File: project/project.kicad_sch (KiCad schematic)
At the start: 174 parts

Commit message: adding more things
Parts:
- removed Cs19, Cs20: chair s, -local:chair_small, symbol Device:R
- removed R83: clean clothes, -local:_o_clean_clothes__, symbol Device:R
- added R12: Painting table, -local:_o_painting_table__, symbol Device:R
- added R20: palet rack2, -local:_o_palet_rack__, symbol Device:R
- added R21: Broken tools, -local:_o_broken_tools_shelf__, symbol Device:R
- added R22: Strings and wheels, -local:_o_strings_wheels_shelf__, symbol Device:R
- added R39: cube container, -local:_o_cube_container__, symbol Device:R
- added R45: Trash el, -local:_o_trash_electronics__, symbol Device:R
- added R55: Dirty small table, -local:_o_dirty_small_table__, symbol Device:R
- added R58: Presentation chairs, -local:_o_chair_box__, symbol Device:R
- added R65: Lightbox, -local:_e_lightbox__, symbol Device:R
- added R80: el center shitty table, -local:_e_shitty_table__, symbol Device:R
- R19: renamed from R35; value palet rack -> palet rack1
- R68: renamed from R78; footprint -local:_e_kitchen_table2__ -> -local:_e_shitty_table__
- R73: renamed from R69; footprint -local:_e_lab_table_x3__ -> -local:_e_lab_table_normal__
- R74: renamed from R70; footprint -local:_e_lab_table_x3__ -> -local:_e_lab_table_tall__
- R75: renamed from R71; footprint -local:_e_lab_table_x3__ -> -local:_e_lab_table_tall__
- R78: renamed from R74; footprint -local:_e_center_table2__ -> -local:_e_center_table1__
- R99: renamed from R90; footprint -local:_o_rack__ -> -local:_e_rack__
- renumbered R12 to R13, R13 to R14, R14 to R17, R36 to R18, R19 to R23, R20 to R24, R21 to R25, R22 to R26, R23 to R27, R24 to R28, R25 to R29, R26 to R30, R27 to R31, R28 to R32, R29 to R33, R30 to R34, R31 to R35, R32 to R36, R33 to R37, R34 to R38, R37 to R40, R38 to R41, R39 to R42, R40 to R43, R41 to R44, R42 to R46, R43 to R47, R44 to R48, R45 to R49, R46 to R50, R47 to R51, R48 to R52, R18 to R53, R17 to R54, R49 to R56, R50 to R57, R51 to R59, R52 to R60, R53 to R61, R54 to R62, R55 to R63, R56 to R64, R76 to R66, R77 to R67, R79 to R69, R80 to R70, R81 to R71, R82 to R72, R72 to R76, R73 to R77, R75 to R79, R57 to R81, R58 to R82, R59 to R83, R60 to R84, R61 to R85, R62 to R86, R63 to R87, R64 to R88, R65 to R89, R66 to R90, R67 to R91, R68 to R92, R84 to R93, R85 to R94, R86 to R95, R87 to R96, R88 to R97, R89 to R98

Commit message: moving things around
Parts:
- removed Be8: bench, -local:_e_bench__, symbol Device:R
- removed R34: hammers, -local:_o_thin_shelf__, symbol Device:R
- removed R38: files, -local:_o_thick_shelf__, symbol Device:R
- removed R64: Ceiling shelf, -local:_e_ceiling_shelf__, symbol Device:R
- removed R92: el6 t, -local:_o_wheel_tower3__, symbol Device:R
- added R33: clamps, -local:_o_clamps__, symbol Device:R
- added R35: cube container, -local:_o_cube_container_x2__, symbol Device:R
- added R39, R40: palet rack, -local:_o_palet_rack_x4__, symbol Device:R
- added R44: shitty table, -local:_o_shitty_table_x4__, symbol Device:R
- added R47: trash bucket, -local:_o_trash_bucket_x2__, symbol Device:R
- added R5: cnc router, -local:_o_cnc_mill__, symbol Device:R
- Be1, Be2, Be3, Be4, Be5, Be6, Be7: footprint -local:_e_bench__ -> -local:_e_bench_x7__
- R14: renamed from R13; footprint -local:_o_thin_shelf__ -> -local:_o_thin_shelf_single__; new (none) -> yes
- R19: renamed from R23; footprint -local:_o_wheel_tower2__ -> -local:_o_wheel_tower2_x7__
- R29: renamed from R33; footprint -local:_o_thin_shelf__ -> -local:_o_thin_shelf_x2__
- R3: footprint -local:_o_wheel_tower2__ -> -local:_o_wheel_tower2_x7__; new (none) -> yes
- R30: renamed from R35; footprint -local:_o_thin_shelf__ -> -local:_o_thin_shelf_x2__
- R31: renamed from R37; value ppe -> ppe and files
- R32: renamed from R36; footprint -local:_o_thin_shelf__ -> -local:_o_thin_shelf_single__
- R34: renamed from R39; footprint -local:_o_cube_container__ -> -local:_o_cube_container_x2__
- R37: renamed from R19; value palet rack1 -> palet rack; footprint -local:_o_palet_rack__ -> -local:_o_palet_rack_x4__
- R38: renamed from R20; value palet rack2 -> palet rack; footprint -local:_o_palet_rack__ -> -local:_o_palet_rack_x4__
- R43: value trash bottles -> shitty table; footprint -local:_o_trash_bottles__ -> -local:_o_shitty_table_x4__
- R46: renamed from R41; footprint -local:_o_trash_bucket__ -> -local:_o_trash_bucket_x2__
- R51: renamed from R46; footprint -local:_o_wheel_tower1__ -> -local:_o_wheel_tower1_x7__
- R52: renamed from R47; footprint -local:_o_wheel_tower1__ -> -local:_o_wheel_tower1_x7__
- R53: renamed from R48; footprint -local:_o_wheel_tower1__ -> -local:_o_wheel_tower1_x7__
- R54: renamed from R49; footprint -local:_o_wheel_tower1__ -> -local:_o_wheel_tower1_x7__
- R55: renamed from R50; footprint -local:_o_wheel_tower1__ -> -local:_o_wheel_tower1_x7__
- R56: renamed from R51; footprint -local:_o_wheel_tower1__ -> -local:_o_wheel_tower1_x7__
- R57: renamed from R52; footprint -local:_o_wheel_tower1__ -> -local:_o_wheel_tower1_x7__
- R72: renamed from R68; footprint -local:_e_shitty_table__ -> -local:_o_shitty_table_x4__
- R78: renamed from R74; footprint -local:_e_lab_table_tall__ -> -local:_e_lab_table_tall_x2__
- R79: renamed from R75; footprint -local:_e_lab_table_tall__ -> -local:_e_lab_table_tall_x2__
- R80: renamed from R76; footprint -local:_e_center_table1__ -> -local:_e_center_table1_x3__
- R81: renamed from R77; footprint -local:_e_center_table1__ -> -local:_e_center_table1_x3__
- R82: renamed from R78; footprint -local:_e_center_table1__ -> -local:_e_center_table1_x3__
- R84: renamed from R80; footprint -local:_e_shitty_table__ -> -local:_o_shitty_table_x4__
- R85: renamed from R81; footprint -local:_o_wheel_tower2__ -> -local:_o_wheel_tower2_x7__
- R86: renamed from R82; footprint -local:_o_wheel_tower2__ -> -local:_o_wheel_tower2_x7__
- R87: renamed from R83; footprint -local:_o_wheel_tower2__ -> -local:_o_wheel_tower2_x7__
- R88: renamed from R84; footprint -local:_o_wheel_tower2__ -> -local:_o_wheel_tower2_x7__
- R89: renamed from R85; footprint -local:_o_wheel_tower2__ -> -local:_o_wheel_tower2_x7__
- R90: renamed from R86; footprint -local:_o_wheel_tower2__ -> -local:_o_wheel_tower2_x7__
- R91: renamed from R87; value el1 t -> el; footprint -local:_o_wheel_tower3__ -> -local:_o_wheel_tower3_x5__
- R92: renamed from R88; value el2 t -> el; footprint -local:_o_wheel_tower3__ -> -local:_o_wheel_tower3_x5__
- R93: renamed from R89; value el3 t -> el; footprint -local:_o_wheel_tower3__ -> -local:_o_wheel_tower3_x5__
- R94: renamed from R90; value el4 t -> el; footprint -local:_o_wheel_tower3__ -> -local:_o_wheel_tower3_x5__
- R95: renamed from R91; value el5 t -> el; footprint -local:_o_wheel_tower3__ -> -local:_o_wheel_tower3_x5__
- renumbered R9 to R10, R97 to R100, R98 to R101, R99 to R102, R10 to R11, R11 to R12, R12 to R13, R14 to R15, R15 to R16, R16 to R17, R17 to R18, R24 to R20, R25 to R21, R26 to R22, R27 to R23, R28 to R24, R29 to R25, R30 to R26, R31 to R27, R32 to R28, R18 to R36, R21 to R41, R22 to R42, R40 to R45, R42 to R48, R44 to R49, R45 to R50, R53 to R58, R54 to R59, R5 to R6, R55 to R60, R56 to R61, R57 to R62, R58 to R63, R59 to R64, R60 to R65, R61 to R66, R62 to R67, R63 to R68, R65 to R69, R6 to R7, R66 to R70, R67 to R71, R69 to R73, R70 to R74, R71 to R75, R72 to R76, R73 to R77, R7 to R8, R79 to R83, R8 to R9, R93 to R96, R94 to R97, R95 to R98, R96 to R99
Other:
- moved on the sheet: Be1, Be2, Be3, Be4, Be5, Be6, Be7, Cb1, Cb10, Cb11, Cb12, Cb13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

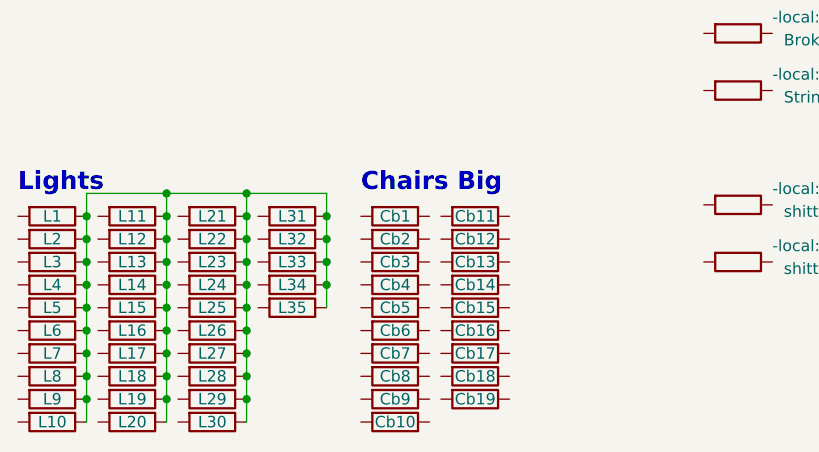
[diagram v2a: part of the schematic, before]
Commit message: adding light and moving electrical stuff
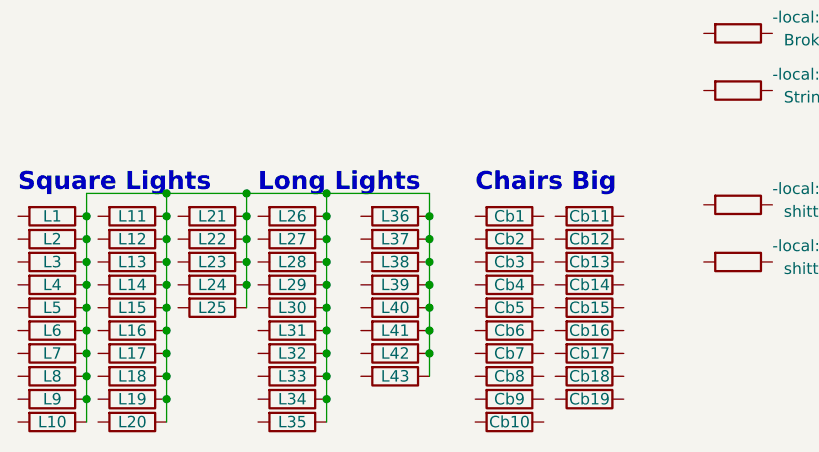
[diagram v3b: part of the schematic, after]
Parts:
- removed L31, L32: light, -local:light_long, symbol Device:R
- added L24, L25: light, -local:light_square, symbol Device:R
- added L34, L35, L38, L39, L40, L41, L42, L43: light, -local:light_long, symbol Device:R
- renumbered L24 to L26, L25 to L27, L26 to L28, L27 to L29, L28 to L30, L29 to L31, L30 to L32, L34 to L36, L35 to L37
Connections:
- net at L1.1, L10.1, L11.1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: now also L24.1, L25.1, L34.1, L35.1, L38.1, L39.1, L40.1, L41.1, L42.1, L43.1
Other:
- note added: "Long Lights"
- note added: "Square Lights"
- note removed: "Lights"
- moved on the sheet: Cb1, Cb10, Cb11, Cb12, Cb13, Cb14, Cb15, Cb16, Cb17, Cb18, Cb19, Cb2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

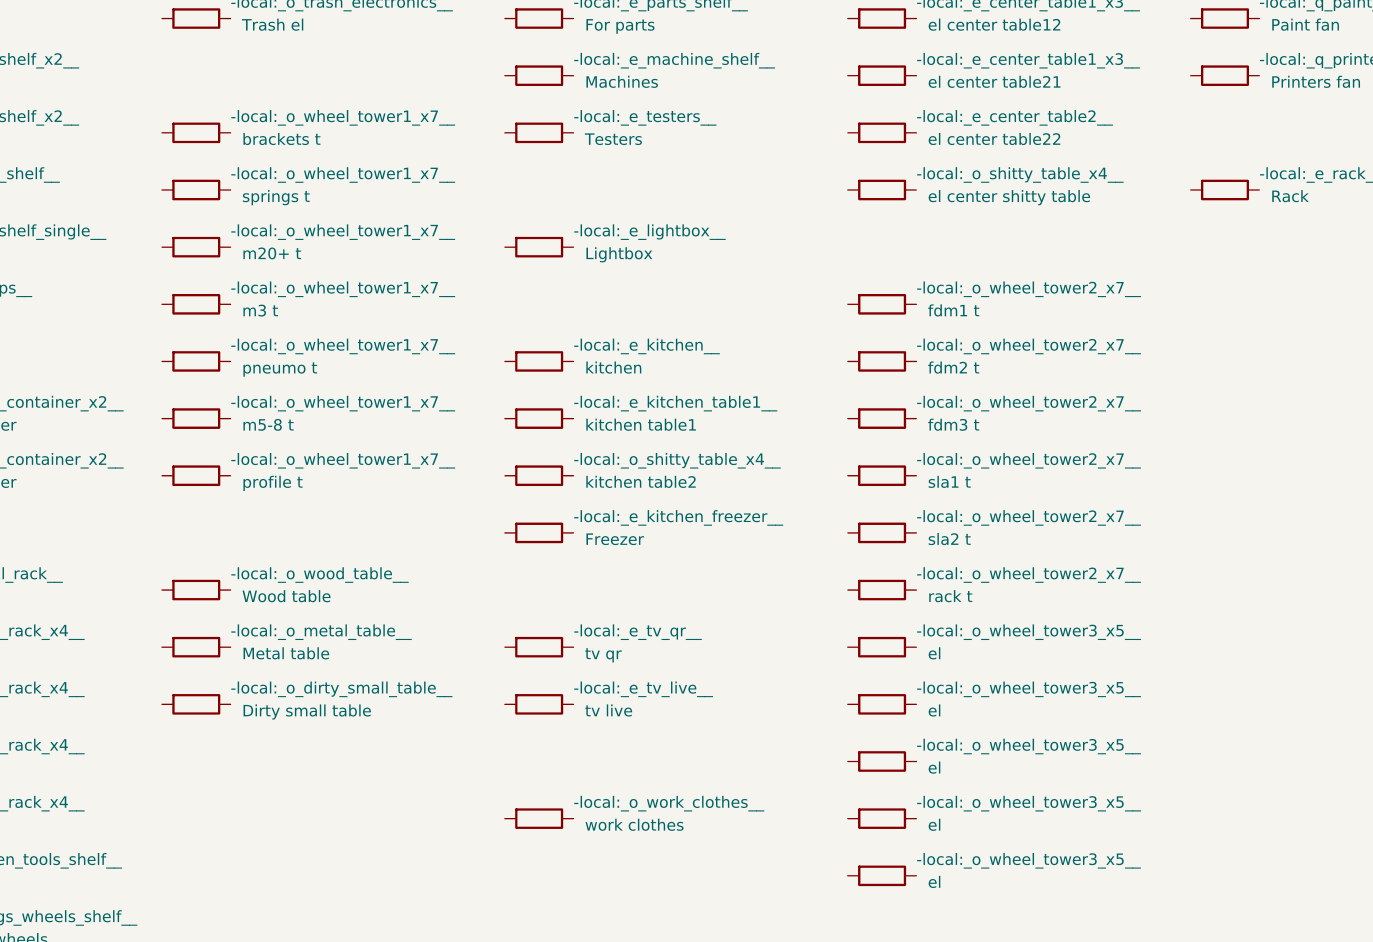
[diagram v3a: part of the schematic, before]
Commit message: reworking dirty workshop
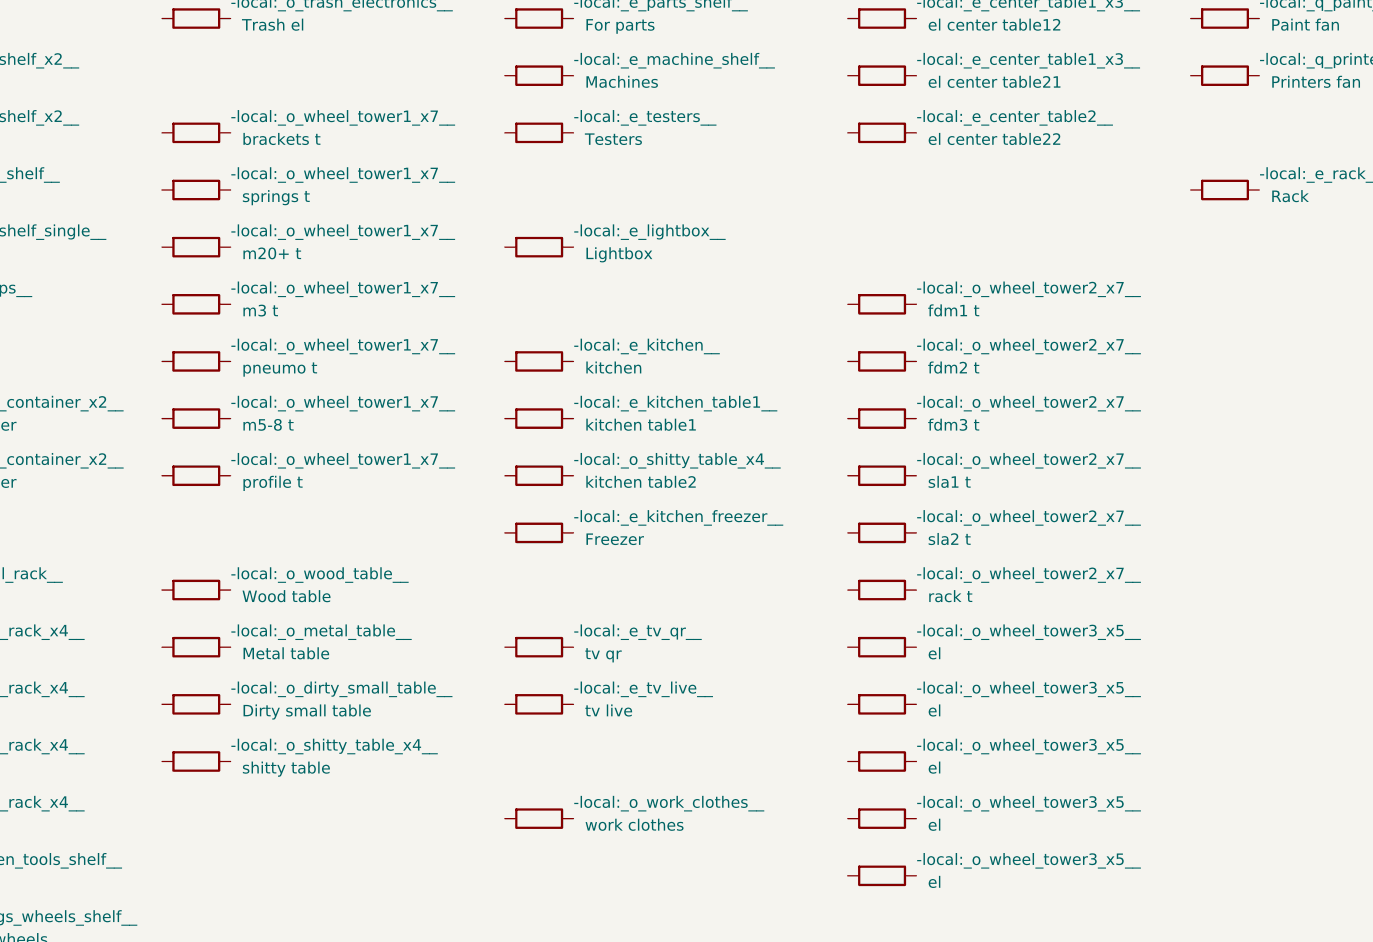
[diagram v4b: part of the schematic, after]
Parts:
- R84: value el center shitty table -> shitty table
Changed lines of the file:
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@@
     (pin "2")
   )
-  (symbol (lib_id "Device:R") (at 207.01 76.2 270) (unit 1)
-    (in_bom yes) (on_board yes)
-    (property "Reference" "R84" (id 0) (at 207.01 67.31 90)
-      (effects (font (size 1.27 1.27)) hide)
-    )
-    (property "Value" "el center shitty table" (id 1) (at 212.09 76.2 90)
-      (effects (font (size 1.27 1.27)) (justify left top))
-    )
-    (property "Footprint" "-local:_o_shitty_table_x4__" (id 2) (at 210.82 73.66 90)
-      (effects (font (size 1.27 1.27)) (justify left top))
-    )
-    (property "Datasheet" "~" (id 3) (at 207.01 76.2 0)
+  (symbol (lib_id "Device:R") (at 130.81 139.7 270) (unit 1)
+    (in_bom yes) (on_board yes)
+    (property "Reference" "R84" (id 0) (at 130.81 130.81 90)
+      (effects (font (size 1.27 1.27)) hide)
+    )
+    (property "Value" "shitty table" (id 1) (at 135.89 139.7 90)
+      (effects (font (size 1.27 1.27)) (justify left top))
+    )
+    (property "Footprint" "-local:_o_shitty_table_x4__" (id 2) (at 134.62 137.16 90)
+      (effects (font (size 1.27 1.27)) (justify left top))
+    )
+    (property "Datasheet" "~" (id 3) (at 130.81 139.7 0)
       (effects (font (size 1.27 1.27)) hide)
     )
@@
     )
     (path "/ee8eb108-7b7e-4287-afee-5be254206bcc"
-      (reference "R84") (unit 1) (value "el center shitty table") (footprint "-local:_o_shitty_table_x4__")
+      (reference "R84") (unit 1) (value "shitty table") (footprint "-local:_o_shitty_table_x4__")
     )
     (path "/8ea05b75-2459-4fce-bd02-bcc5ee2dfb79"
